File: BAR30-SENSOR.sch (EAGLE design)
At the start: 16 parts, among them Q1 BSS138, Q2 BSS138

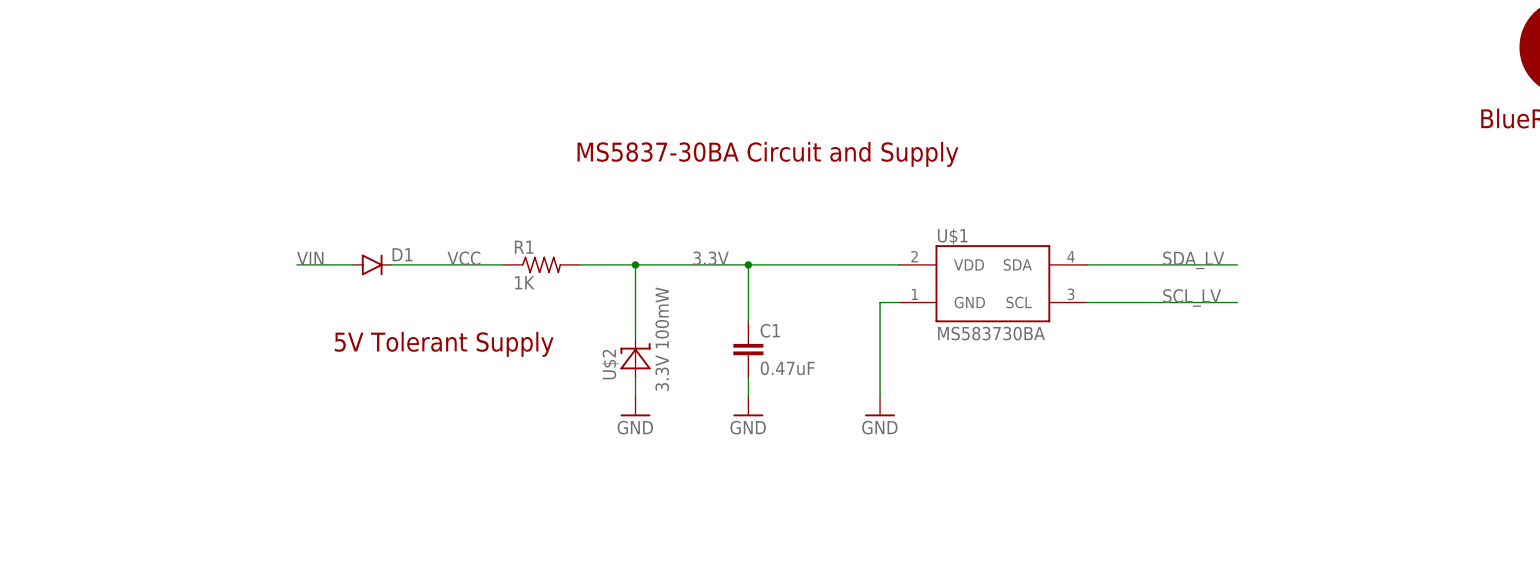
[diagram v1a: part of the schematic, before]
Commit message: Change voltage regulator from zener to LDO.
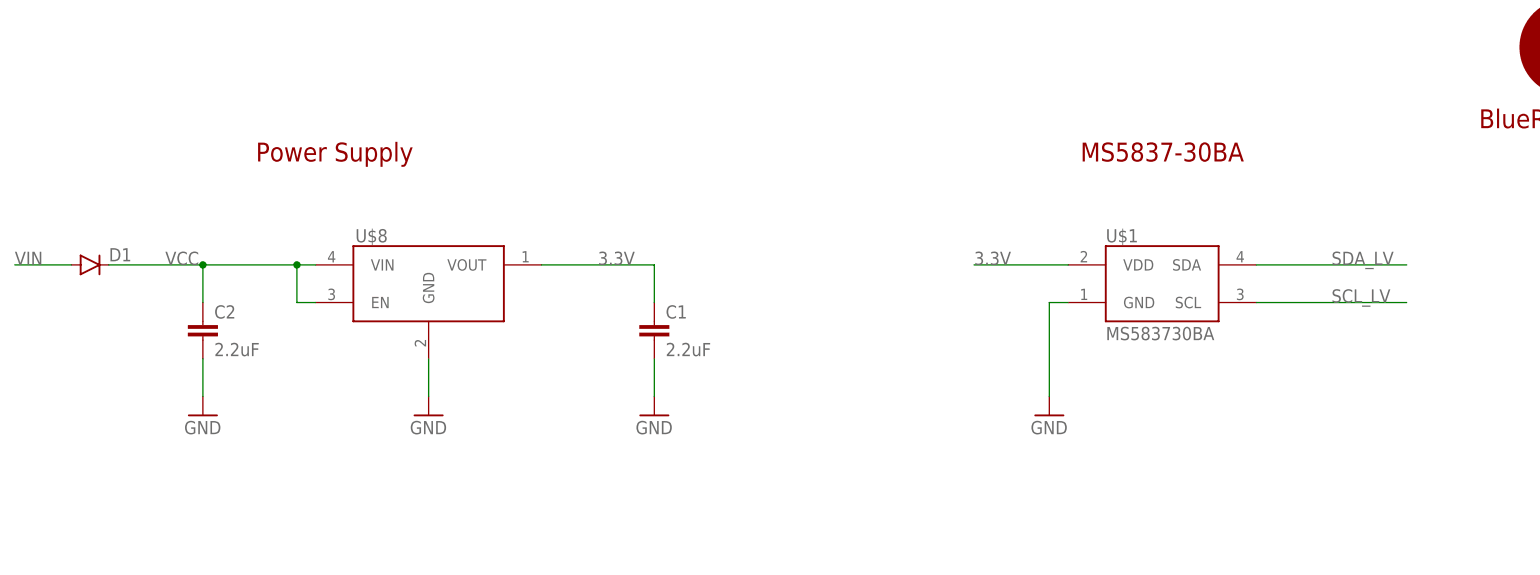
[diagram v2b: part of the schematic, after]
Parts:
- removed R1: 1K, resistor:R-US_R0402
- removed U$2: 3.3V 100mW, BR-Eagle-Library:DIODE-ZENER0603/SOD-523
- added C2: 2.2uF, resistor:C-EUC0402
- added U$8: VREG-MIC5365, BlueRobotics-Main:VREG-MIC5365
- C1: value 0.47uF -> 2.2uF
- U$7: value LOGOBR-LOGO-M -> LOGOBR-LOGO-S; device BR-Eagle-Library:LOGOBR-LOGO-M -> BR-Eagle-Library:LOGOBR-LOGO-S
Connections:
- net 3.3V: now also U$8.VOUT; no longer R1.2, U$2.C
- net GND: now also C2.2, U$8.GND; no longer U$2.A
- net VCC: now also C2.1, U$8.EN, U$8.VIN; no longer R1.1
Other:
- note added: "MS5837-30BA"
- note added: "Power Supply"
- note removed: "5V Tolerant Supply"
- note removed: "MS5837-30BA Circuit and Supply"
- moved on the sheet: C1, D1, U$1

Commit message: Fixed incorrect regulator footprint.
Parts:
- C1, C2: value 2.2uF -> 1uF
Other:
- note added: "MIC5365"
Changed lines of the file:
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@@
 <grid distance="0.1" unitdist="inch" unit="inch" style="lines" multiple="1" display="no" altdistance="0.01" altunitdist="inch" altunit="inch"/>
 <layers>
-<layer number="1" name="Top" color="4" fill="1" visible="yes" active="no"/>
-<layer number="2" name="Route2" color="1" fill="3" visible="yes" active="no"/>
-<layer number="3" name="Route3" color="4" fill="3" visible="yes" active="no"/>
-<layer number="14" name="Route14" color="1" fill="6" visible="yes" active="no"/>
-<layer number="15" name="Route15" color="4" fill="6" visible="yes" active="no"/>
-<layer number="16" name="Bottom" color="1" fill="1" visible="yes" active="no"/>
-<layer number="17" name="Pads" color="2" fill="1" visible="yes" active="no"/>
-<layer number="18" name="Vias" color="2" fill="1" visible="yes" active="no"/>
-<layer number="19" name="Unrouted" color="6" fill="1" visible="yes" active="no"/>
-<layer number="20" name="Dimension" color="15" fill="1" visible="yes" active="no"/>
-<layer number="21" name="tPlace" color="7" fill="1" visible="yes" active="no"/>
-<layer number="22" name="bPlace" color="7" fill="1" visible="yes" active="no"/>
-<layer number="23" name="tOrigins" color="15" fill="1" visible="yes" active="no"/>
-<layer number="24" name="bOrigins" color="15" fill="1" visible="yes" active="no"/>
-<layer number="25" name="tNames" color="7" fill="1" visible="yes" active="no"/>
-<layer number="26" name="bNames" color="7" fill="1" visible="yes" active="no"/>
-<layer number="27" name="tValues" color="7" fill="1" visible="yes" active="no"/>
-<layer number="28" name="bValues" color="7" fill="1" visible="yes" active="no"/>
+<layer number="1" name="Top" color="4" fill="1" visible="no" active="no"/>
+<layer number="2" name="Route2" color="1" fill="3" visible="no" active="no"/>
+<layer number="3" name="Route3" color="4" fill="3" visible="no" active="no"/>
+<layer number="14" name="Route14" color="1" fill="6" visible="no" active="no"/>
+<layer number="15" name="Route15" color="4" fill="6" visible="no" active="no"/>
+<layer number="16" name="Bottom" color="1" fill="1" visible="no" active="no"/>
+<layer number="17" name="Pads" color="2" fill="1" visible="no" active="no"/>
+<layer number="18" name="Vias" color="2" fill="1" visible="no" active="no"/>
+<layer number="19" name="Unrouted" color="6" fill="1" visible="no" active="no"/>
+<layer number="20" name="Dimension" color="15" fill="1" visible="no" active="no"/>
+<layer number="21" name="tPlace" color="7" fill="1" visible="no" active="no"/>
+<layer number="22" name="bPlace" color="7" fill="1" visible="no" active="no"/>
+<layer number="23" name="tOrigins" color="15" fill="1" visible="no" active="no"/>
+<layer number="24" name="bOrigins" color="15" fill="1" visible="no" active="no"/>
+<layer number="25" name="tNames" color="7" fill="1" visible="no" active="no"/>
+<layer number="26" name="bNames" color="7" fill="1" visible="no" active="no"/>
+<layer number="27" name="tValues" color="7" fill="1" visible="no" active="no"/>
+<layer number="28" name="bValues" color="7" fill="1" visible="no" active="no"/>
 <layer number="29" name="tStop" color="7" fill="3" visible="no" active="no"/>
 <layer number="30" name="bStop" color="7" fill="6" visible="no" active="no"/>
@@
 <layer number="35" name="tGlue" color="7" fill="4" visible="no" active="no"/>
 <layer number="36" name="bGlue" color="7" fill="5" visible="no" active="no"/>
-<layer number="37" name="tTest" color="7" fill="1" visible="yes" active="no"/>
-<layer number="38" name="bTest" color="7" fill="1" visible="yes" active="no"/>
+<layer number="37" name="tTest" color="7" fill="1" visible="no" active="no"/>
+<layer number="38" name="bTest" color="7" fill="1" visible="no" active="no"/>
 <layer number="39" name="tKeepout" color="4" fill="11" visible="no" active="no"/>
 <layer number="40" name="bKeepout" color="1" fill="11" visible="no" active="no"/>
@@
 <layer number="44" name="Drills" color="7" fill="1" visible="no" active="no"/>
 <layer number="45" name="Holes" color="7" fill="1" visible="no" active="no"/>
-<layer number="46" name="Milling" color="3" fill="1" visible="yes" active="no"/>
-<layer number="47" name="Measures" color="7" fill="1" visible="yes" active="no"/>
-<layer number="48" name="Document" color="7" fill="1" visible="yes" active="no"/>
-<layer number="49" name="Reference" color="7" fill="1" visible="yes" active="no"/>
-<layer number="50" name="dxf" color="7" fill="1" visible="yes" active="no"/>
-<layer number="51" name="tDocu" color="7" fill="1" visible="yes" active="no"/>
-<layer number="52" name="bDocu" color="7" fill="1" visible="yes" active="no"/>
-<layer number="53" name="tGND_GNDA" color="7" fill="9" visible="yes" active="no"/>
-<layer number="54" name="bGND_GNDA" color="1" fill="9" visible="yes" active="no"/>
-<layer number="56" name="wert" color="7" fill="1" visible="yes" active="no"/>
-<layer number="57" name="tCAD" color="7" fill="1" visible="yes" active="no"/>
+<layer number="46" name="Milling" color="3" fill="1" visible="no" active="no"/>
+<layer number="47" name="Measures" color="7" fill="1" visible="no" active="no"/>
+<layer number="48" name="Document" color="7" fill="1" visible="no" active="no"/>
+<layer number="49" name="Reference" color="7" fill="1" visible="no" active="no"/>
+<layer number="50" name="dxf" color="7" fill="1" visible="no" active="no"/>
+<layer number="51" name="tDocu" color="7" fill="1" visible="no" active="no"/>
+<layer number="52" name="bDocu" color="7" fill="1" visible="no" active="no"/>
+<layer number="53" name="tGND_GNDA" color="7" fill="9" visible="no" active="no"/>
+<layer number="54" name="bGND_GNDA" color="1" fill="9" visible="no" active="no"/>
+<layer number="56" name="wert" color="7" fill="1" visible="no" active="no"/>
+<layer number="57" name="tCAD" color="7" fill="1" visible="no" active="no"/>
 <layer number="90" name="Modules" color="5" fill="1" visible="yes" active="yes"/>
 <layer number="91" name="Nets" color="2" fill="1" visible="yes" active="yes"/>
@@
 <parts>
 <part name="U$1" library="BR-Eagle-Library" deviceset="MS5837" device="30BA"/>
-<part name="C1" library="resistor" deviceset="C-EU" device="C0402" value="2.2uF"/>
+<part name="C1" library="resistor" deviceset="C-EU" device="C0402" value="1uF"/>
 <part name="GND1" library="supply1" deviceset="GND" device=""/>
 <part name="GND2" library="supply1" deviceset="GND" device=""/>
@@
 <part name="U$7" library="BR-Eagle-Library" deviceset="LOGO" device="BR-LOGO-S" value="LOGOBR-LOGO-S"/>
 <part name="U$8" library="BlueRobotics-Main" deviceset="VREG-MIC5365" device=""/>
-<part name="C2" library="resistor" deviceset="C-EU" device="C0402" value="2.2uF"/>
+<part name="C2" library="resistor" deviceset="C-EU" device="C0402" value="1uF"/>
 <part name="GND4" library="supply1" deviceset="GND" device=""/>
 </parts>
@@
 <text x="78.74" y="71.12" size="2.54" layer="94" align="center">MS5837-30BA</text>
 <text x="-33.02" y="71.12" size="2.54" layer="94" align="center">Power Supply</text>
+<text x="-15.24" y="43.18" size="1.778" layer="97">MIC5365</text>
 </plain>
 <instances>

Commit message: Added PDF schematic, updated readme.
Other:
- note removed: "BAR30 Pressure Sensor"
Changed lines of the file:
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@@
 <sheet>
 <plain>
-<text x="52.578" y="-61.722" size="3.81" layer="94">BAR30 Pressure Sensor</text>
 <text x="-33.02" y="2.54" size="2.54" layer="94" align="center">Level Converters for 5V Tolerance</text>
 <text x="83.82" y="2.54" size="2.54" layer="94" align="center">Solder Pad Connections</text>

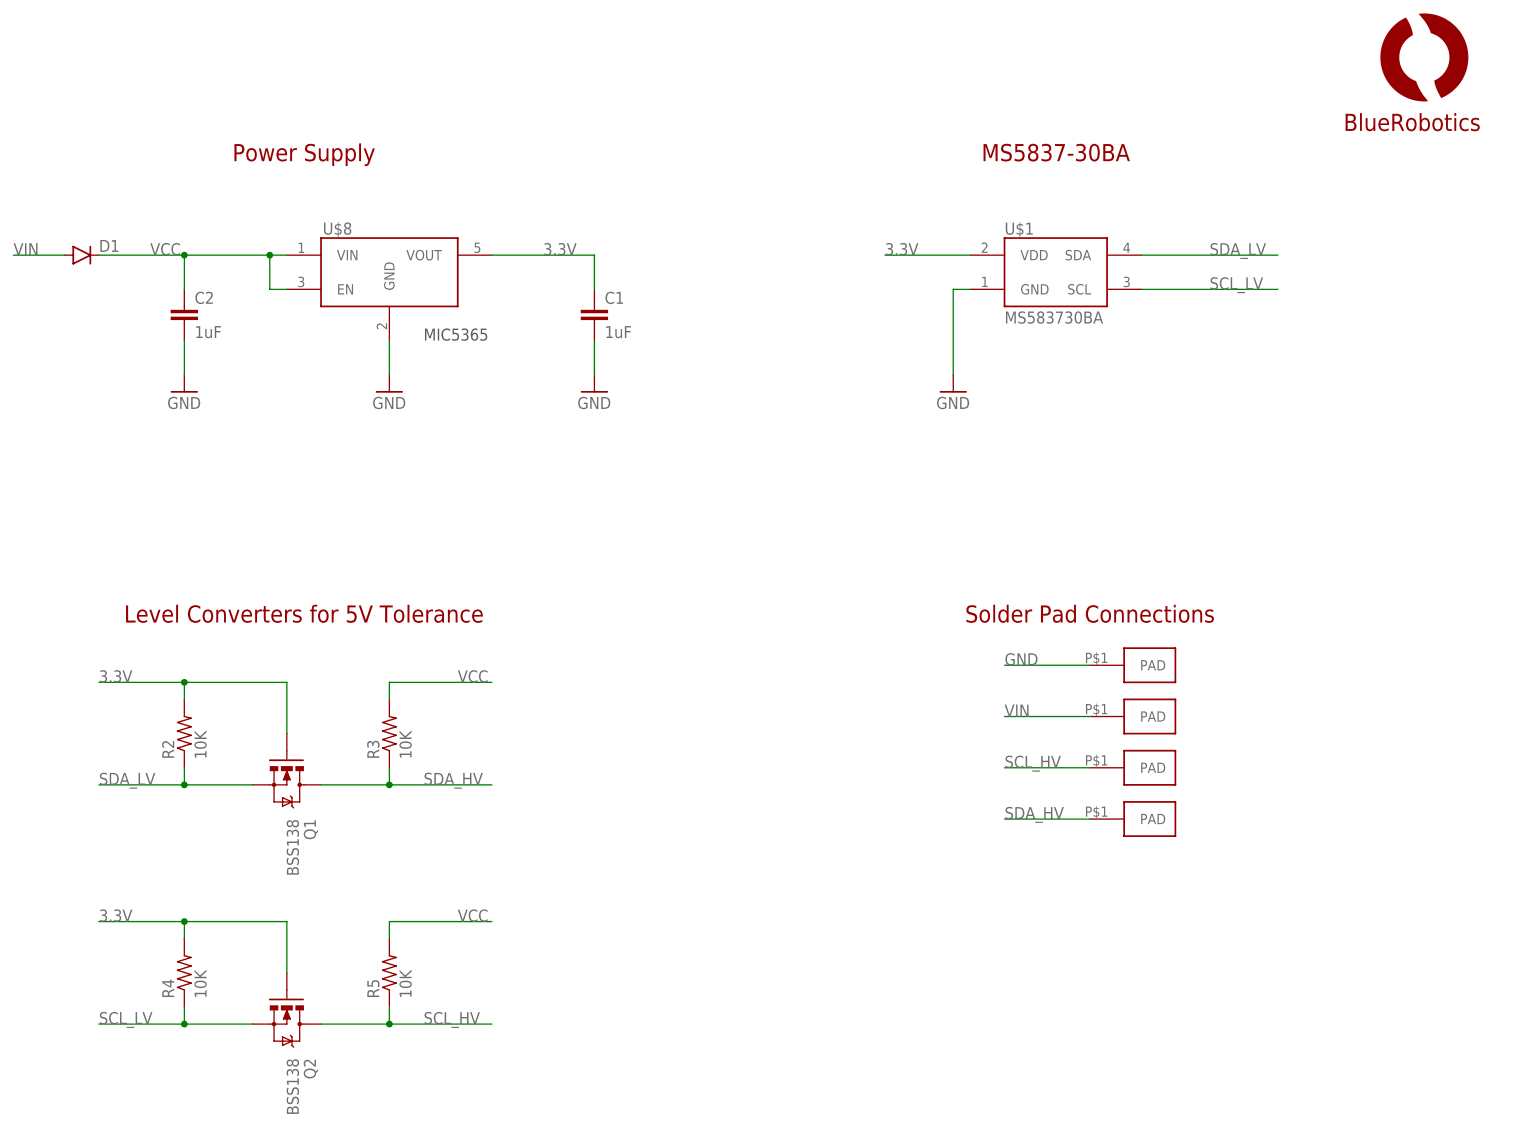
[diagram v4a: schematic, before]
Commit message: Last minute major redesign for DroneCode I2C compatibility.
PixHawk and others cannot handle 5V I2C logic but have 5V I2C power supplies!
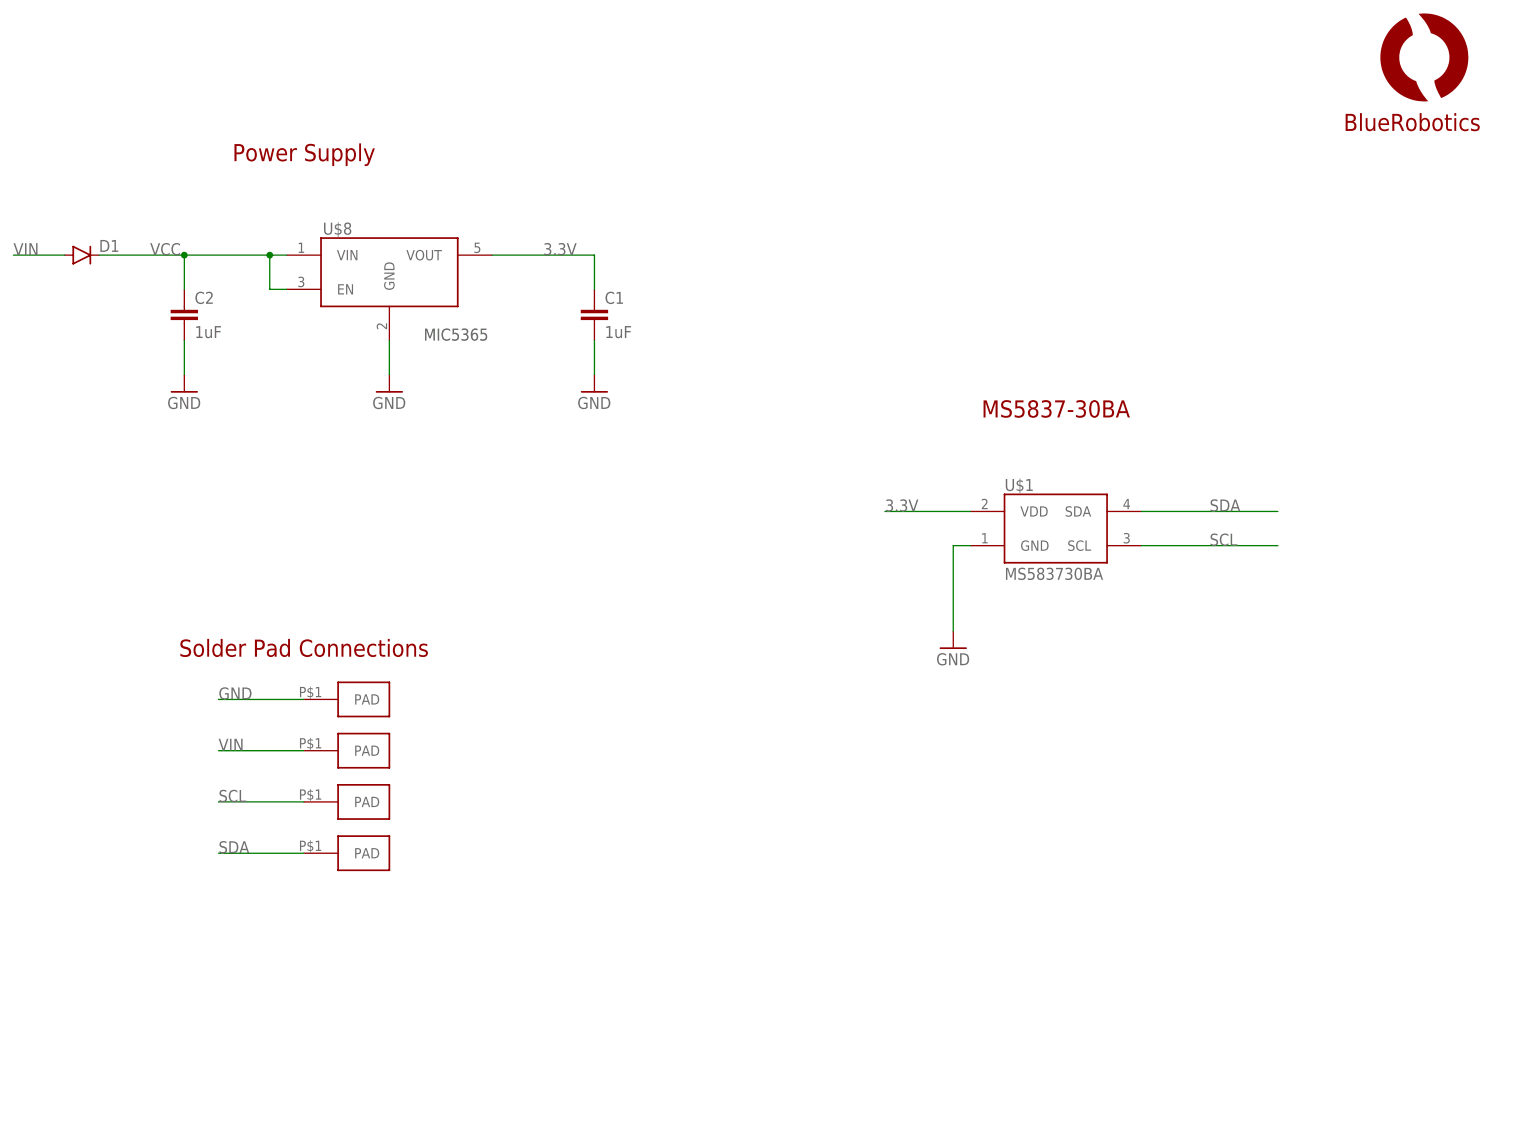
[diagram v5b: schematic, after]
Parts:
- removed Q1, Q2: BSS138, SparkFun-DiscreteSemi:MOSFET-NCHANNEL2N7002PW
- removed R2, R3, R4, R5: 10K, resistor:R-US_R0402
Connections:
- removed net SCL_HV: Q2.D, R5.1, U$5.PAD
- removed net SCL_LV: Q2.S, R4.1, U$1.SCL
- removed net SDA_HV: Q1.D, R3.1, U$6.PAD
- removed net SDA_LV: Q1.S, R2.1, U$1.SDA
- new net SCL: U$1.SCL, U$5.PAD
- new net SDA: U$1.SDA, U$6.PAD
- net 3.3V: no longer Q1.G, Q2.G, R2.2, R4.2
- net VCC: no longer R3.2, R5.2
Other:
- note removed: "Level Converters for 5V Tolerance"
- moved on the sheet: U$1
